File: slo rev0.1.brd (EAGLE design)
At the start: 100 x 100 mm, 12 parts, among them IC2 TB6612FNG, IC6 A1202LH, IC7 A1202LH, IC8 A1202LH, IC9 A1202LH

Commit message: added more goodies
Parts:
- added C5, C6: (no value), resistor:C1206
- added C7: 2.2uF, clackboard_lib:0603_TANTALUM_CAPACITOR
- added C8: 470pF, resistor:C0603
- added CN1: (no value), adafruit:DCJACK_2MM_PTH
- added JP4: (no value), adafruit:1X06-3.5MM
- added JP5: JUMPER-SMT_2_NO_SILK, SparkFun-Jumpers:SMT-JUMPER_2_NO_SILK
- added JP6: JUMPER-SMT_3_NO_SILK, SparkFun-Jumpers:SMT-JUMPER_3_NO_SILK
- added Q1: 2.5A/30V/105mΩ, SparkFun-DiscreteSemi:SOT23-3
- added R1: 10K, resistor:R1206
- added U1: MIC5219 3.3V, SparkFun-IC-Power:SOT23-5
- JP2: device adafruit:1X08-3.5MM -> adafruit:1X06-3.5MM
- moved JP1 159.0 mm to (20.0, 120.0), turned to 90 degrees
- moved IC2 85.0 mm to (85.0, 97.5), turned to 90 degrees
- moved JP2 78.9 mm to (95.3, 97.5), turned to 90 degrees
- moved C1 70.7 mm to (7.20, 49.5)
- moved C2 70.7 mm to (47.2, 89.5)
- moved C4 70.7 mm to (47.2, 9.50)
- moved IC6 70.7 mm to (50.0, 90.0)
- moved IC7 70.7 mm to (10.0, 50.0)
- moved IC8 70.7 mm to (50.0, 10.0)
- moved IC9 70.7 mm to (90.0, 50.0)
- moved JP3 70.7 mm to (80.0, 80.0)
- moved C3 70.7 mm to (87.1, 49.4)
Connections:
- net VBAT renamed N$8
- removed net +3V3: JP1.24, JP1.3V3
- removed net N$16: IC2.13, IC2.14, IC2.24
- removed net N$18: IC2.10, IC2.3, IC2.4, IC2.9
- removed net N$7: IC2.11, JP2.7
- removed net N$8 (its old number): IC2.12, JP2.8
- new net GNDBREAK: CN1.GNDBREAK
- new net N$17: C8.1, U1.4
- new net VMOTOR: C6.1, IC2.13, IC2.14, IC2.24, JP6.3, Q1.2, U1.1
- net GND: now also C1.2, C2.2, C3.2, C4.2, C5.2, C6.2, C7.-, C8.2, CN1.GND, IC2.10, IC2.3, IC2.4, IC2.9, IC6.3, IC7.3, IC8.3, IC9.3, JP2.3, JP2.4, JP3.6, JP4.6, JP6.1, Q1.1, U1.2
- net N$1: now also IC2.2
- net N$10: now also JP1.23, JP1.RST; no longer C1.2, C2.2, C3.2, C4.2, IC6.3, IC7.3, IC8.3, IC9.3, JP3.6
- net N$15: now also JP5.2; no longer IC2.19
- net N$2: now also IC2.5, IC2.6; no longer IC2.2
- net N$3: now also IC2.7, IC2.8, JP2.5; no longer IC2.5, JP2.3
- net N$4: now also IC2.11, IC2.12, JP2.6; no longer IC2.6, JP2.4
- net N$5: now also CN1.PWR, Q1.3; no longer IC2.7, JP2.5
- net N$6: now also IC2.19, JP5.1, R1.1; no longer IC2.8, JP2.6
- net N$9: now also JP6.2, U1.3; no longer C1.1, C2.1, C3.1, C4.1, IC6.1, IC7.1, IC8.1, IC9.1, JP3.1
- net OUT1: now also JP1.19, JP1.D6, JP4.2
- net OUT2: now also JP1.18, JP1.D5, JP4.3
- net OUT3: now also JP1.17, JP1.D4, JP4.4
- net OUT4: now also JP1.16, JP1.D3, JP4.5
- net VCC: now also C1.1, C2.1, C3.1, C4.1, C5.1, C7.+, IC6.1, IC7.1, IC8.1, IC9.1, JP1.24, JP1.3V3, JP3.1, JP4.1, R1.2, U1.5
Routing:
- net VCC: track 0.00 -> 390.3 mm, vias 0 -> 7
- net N$9: track 237.0 -> 2.91 mm, vias 4 -> 0
- net OUT4: track 36.3 -> 192.2 mm, vias 0 -> 1
- net OUT3: track 92.2 -> 241.8 mm, vias 0 -> 1
- net OUT2: track 91.2 -> 237.6 mm, vias 0 -> 1
- net OUT1: track 31.1 -> 173.3 mm, vias 0 -> 1
- net N$15: track 0.00 -> 73.1 mm, vias 0 -> 1
- net N$14: track 0.00 -> 72.0 mm
- net N$12: track 0.00 -> 69.5 mm
- net N$13: track 0.00 -> 69.3 mm
- net N$11: track 0.00 -> 66.5 mm
- net VMOTOR: track 0.00 -> 31.5 mm, vias 0 -> 2
- net GND: track 0.00 -> 30.0 mm, vias 0 -> 14
- net N$8 (its old number): track 14.6 -> 0.00 mm
- net N$5: track 6.97 -> 20.4 mm
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- added copper zone on layer 1, net GND
- added copper zone on layer 16, net GND
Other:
- board size 100 x 100 mm -> 100 x 140 mm

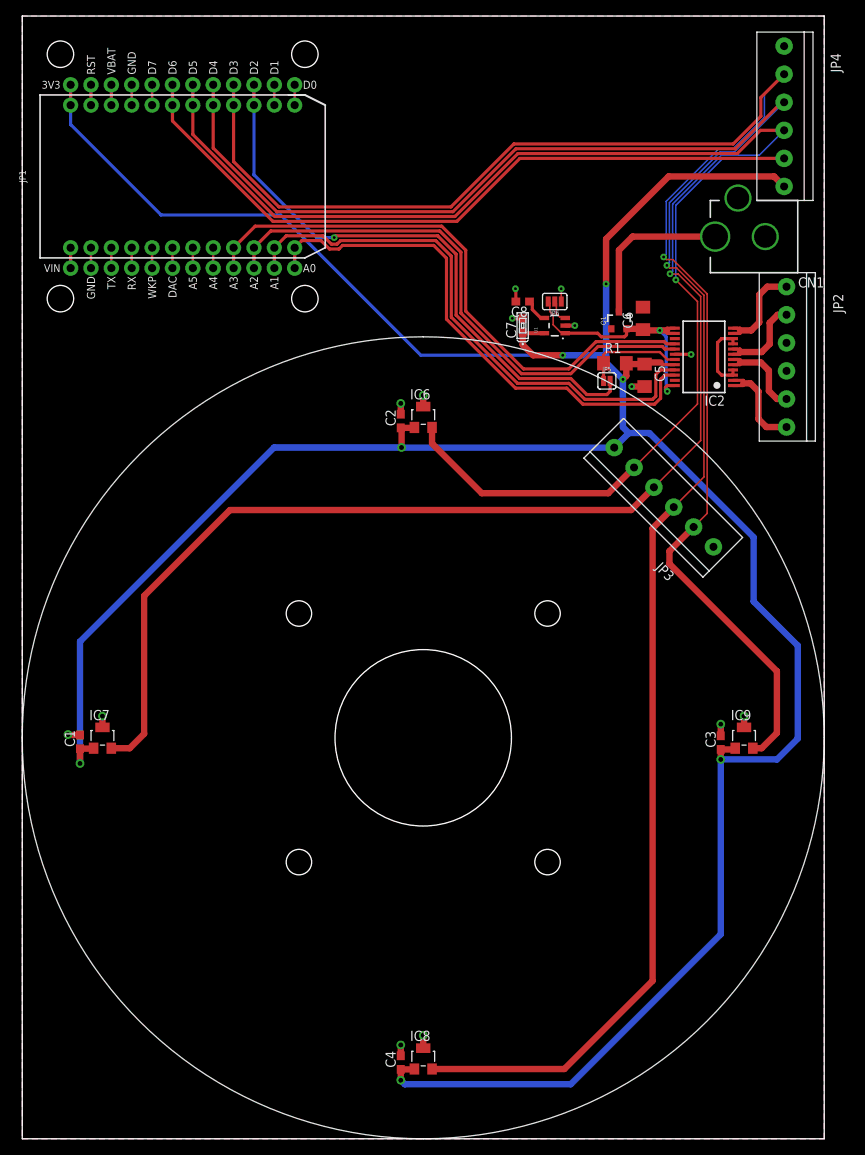
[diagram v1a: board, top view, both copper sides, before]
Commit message: removed a hall sensor
need to create option to house an encoder
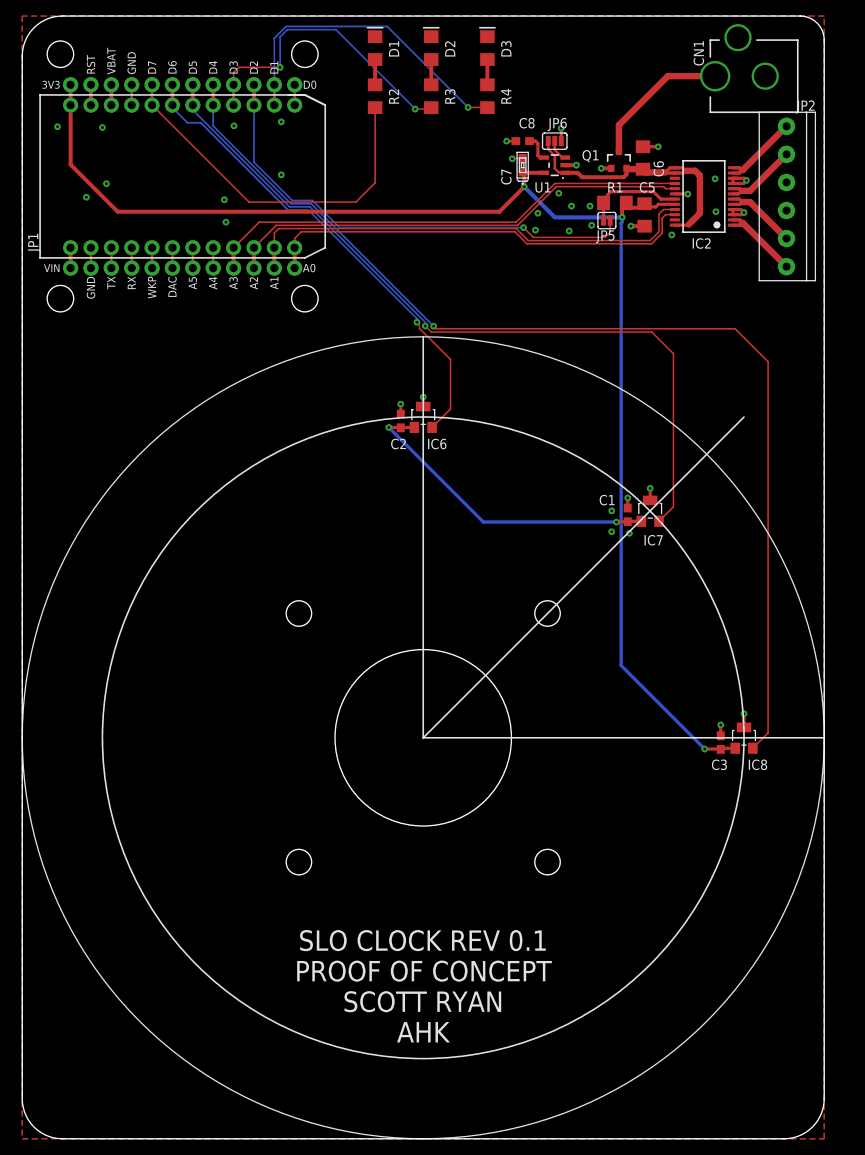
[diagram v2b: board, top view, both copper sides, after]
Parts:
- removed C4: 0.1uF, resistor:C0603
- removed IC9: A1202LH, allegro:SOT23-W
- removed JP3, JP4: (no value), adafruit:1X06-3.5MM
- added D1, D2, D3: (no value), SparkFun-LED:FKIT-LED-1206
- added R2, R3, R4: 100R, resistor:R1206
- moved C1 73.9 mm to (75.5, 77.8)
- moved IC7 73.9 mm to (78.3, 78.3)
- moved IC8 56.6 mm to (90.0, 50.0)
- moved C5 20.0 mm to (77.6, 115.2)
- moved C6 20.0 mm to (77.4, 122.3)
- moved C7 20.0 mm to (62.4, 121.4)
- moved C8 20.0 mm to (62.4, 124.4)
- moved CN1 20.0 mm to (100.0, 132.5)
- moved IC2 20.0 mm to (85.0, 117.5)
- moved JP2 20.0 mm to (95.3, 117.5)
- moved JP5 20.0 mm to (72.9, 114.5)
- moved JP6 20.0 mm to (66.4, 124.4)
- moved Q1 20.0 mm to (74.4, 122.0)
- moved R1 20.0 mm to (73.9, 116.7)
- moved U1 20.0 mm to (66.4, 121.4)
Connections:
- removed net OUT4: IC9.2, JP1.16, JP1.D3, JP3.5, JP4.5
- new net LED1: JP1.20, JP1.D7, R2.1
- new net LED2: JP1.16, JP1.D3, R3.1
- new net LED3: JP1.14, JP1.D1, R4.1
- new net N$16: D2.A, R3.2
- new net N$18: D3.A, R4.2
- new net N$7: D1.A, R2.2
- net GND: now also D1.C, D2.C, D3.C; no longer C4.2, IC9.3, JP3.6, JP4.6
- net OUT1: no longer JP3.2, JP4.2
- net OUT2: no longer JP3.3, JP4.3
- net OUT3: no longer JP3.4, JP4.4
- net VCC: no longer C4.1, IC9.1, JP3.1, JP4.1
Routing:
- net OUT4: track 192.2 -> 0.00 mm, vias 1 -> 0
- net VCC: track 390.3 -> 212.6 mm, vias 7 -> 5
- net OUT2: track 237.6 -> 97.6 mm
- net OUT1: track 173.3 -> 60.5 mm
- net OUT3: track 241.8 -> 135.5 mm
- net LED1: track 0.00 -> 45.7 mm
- net LED3: track 0.00 -> 39.7 mm, vias 0 -> 1
- net LED2: track 0.00 -> 37.3 mm, vias 0 -> 2
- net N$15: track 73.1 -> 59.7 mm
- net N$11: track 66.5 -> 54.7 mm
- net N$12: track 69.5 -> 58.2 mm
- net N$14: track 72.0 -> 60.9 mm
- net N$13: track 69.3 -> 58.3 mm
- net VMOTOR: track 31.5 -> 35.1 mm, vias 2 -> 0
- net N$7: track 0.00 -> 3.16 mm
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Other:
- outline, holes or cut-outs redrawn
- board text added: "SLO CLOCK REV 0.1 PROOF OF CONCEPT SCOTT RYAN AHK"
